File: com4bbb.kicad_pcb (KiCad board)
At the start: 2 copper layers, 54.6 x 86.4 mm, 51 parts, among them J101 RS485, J102 PWR, P8 BeagleBone_Black_Header, P9 BeagleBone_Black_Header, SW101 Reset, SW102 PWR, U101 ESP32-WROOM-32U, U102 SP3485EN, U103 AT24C512C-SSHD-T, U104 WPMDH1100xx1S

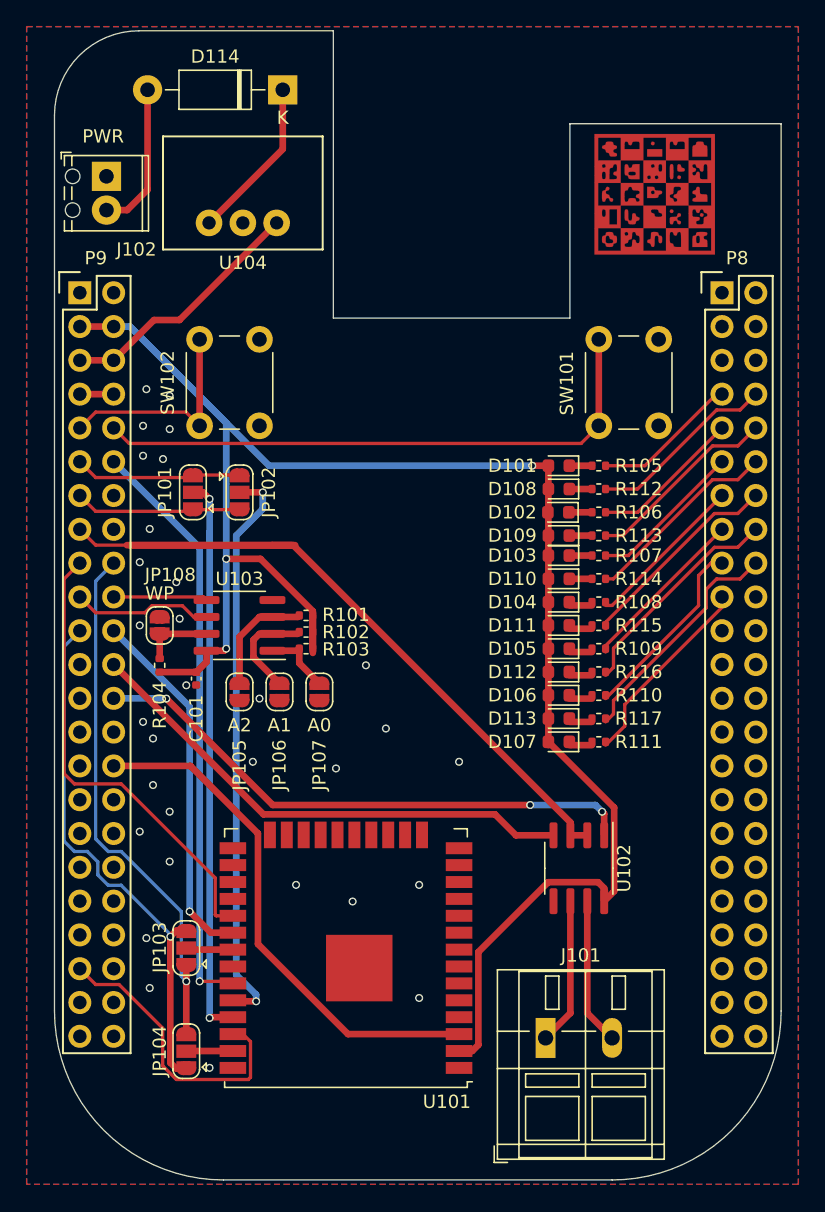
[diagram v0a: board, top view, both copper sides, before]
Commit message: Connect missing boot pin
The ESP32-wroom-32u module use IO0 to enter boot mode. In boot mode
the device can be flashed. Connect IO0 to the Beagle Bone to be able
to update firmware on demand.

Signed-off-by: Benedikt Spranger <b.spranger@linutronix.de>
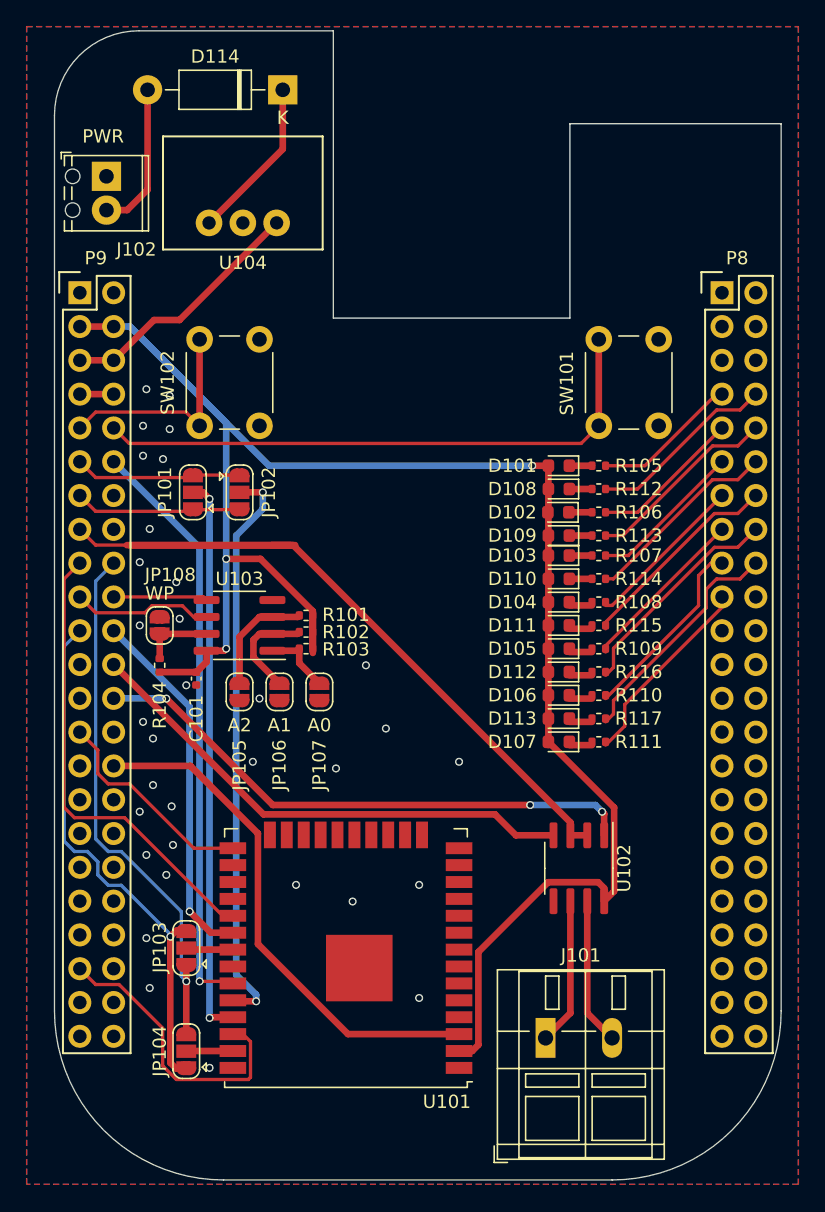
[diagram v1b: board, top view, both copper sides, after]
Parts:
- removed G***: LOGO, eurovibes:LOGO
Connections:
- net /GPIO_112 renamed /GPIO_122
- P9 pad 27: (no net) -> /GPIO_125
- U101 pad 25: (no net) -> /GPIO_125
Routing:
- net /GPIO_125: track 0.00 -> 16.1 mm
- net GNDD: vias 31 -> 33

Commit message: Update to KiCAD version 9
Signed-off-by: Benedikt Spranger <b.spranger@linutronix.de>
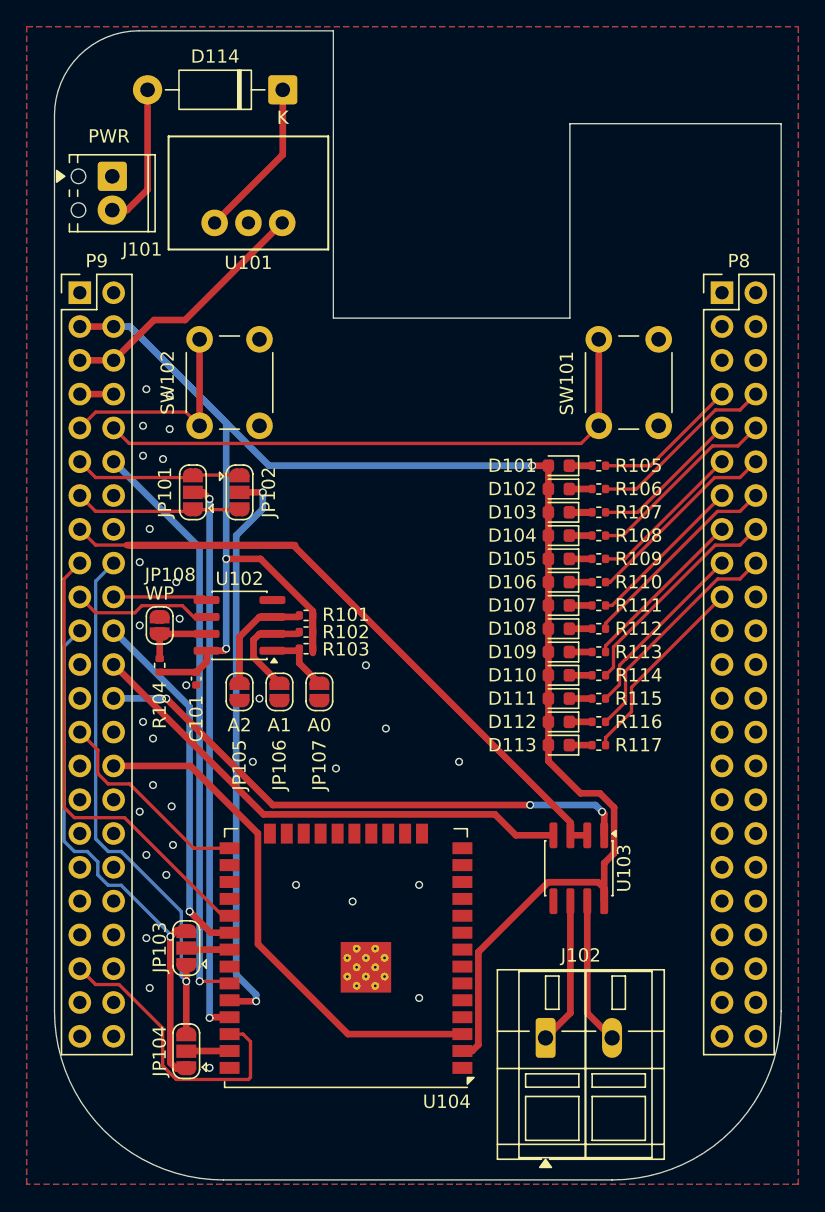
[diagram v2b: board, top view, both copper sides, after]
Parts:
- P8, P9: footprint Socket_BeagleBone_Black:Socket_BeagleBone_Black -> Connector_PinHeader_2.54mm:PinHeader_2x23_P2.54mm_Vertical
- moved D108 10.5 mm to (152.4, 87.6)
- moved R112 10.5 mm to (155.4, 87.6)
- moved D107 10.2 mm to (152.4, 85.9)
- moved R111 10.2 mm to (155.4, 85.9)
- moved D109 8.75 mm to (152.4, 89.4)
- moved R113 8.75 mm to (155.4, 89.4)
- moved D106 8.50 mm to (152.4, 84.1)
- moved R110 8.50 mm to (155.4, 84.1)
- moved D110 7.25 mm to (152.4, 91.1)
- moved R114 7.25 mm to (155.4, 91.1)
- moved D105 6.75 mm to (152.4, 82.4)
- moved R109 6.75 mm to (155.4, 82.4)
- moved D111 5.50 mm to (152.4, 92.9)
- moved R115 5.50 mm to (155.4, 92.9)
- moved D104 5.00 mm to (152.4, 80.6)
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- renumbered J102 to J101, J101 to J102, U104 to U101, U103 to U102, U102 to U103, U101 to U104
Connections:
- P8 pad 10: /LED8 -> /LED3
- P8 pad 11: /LED2 -> /LED4
- P8 pad 12: /LED9 -> /LED5
- P8 pad 13: /LED3 -> /LED6
- P8 pad 14: /LED10 -> /LED7
- P8 pad 15: /LED4 -> /LED8
- P8 pad 16: /LED11 -> /LED9
- P8 pad 17: /LED5 -> /LED10
- P8 pad 18: /LED12 -> /LED11
- P8 pad 19: /LED6 -> /LED12
- P8 pad 20: (no net) -> unconnected-(P8-Pin_20-Pad20)
- P8 pad 21: (no net) -> unconnected-(P8-Pin_21-Pad21)
- P8 pad 22: (no net) -> unconnected-(P8-Pin_22-Pad22)
- P8 pad 23: (no net) -> unconnected-(P8-Pin_23-Pad23)
- P8 pad 24: (no net) -> unconnected-(P8-Pin_24-Pad24)
- P8 pad 25: (no net) -> unconnected-(P8-Pin_25-Pad25)
- P8 pad 26: (no net) -> unconnected-(P8-Pin_26-Pad26)
- P8 pad 27: (no net) -> unconnected-(P8-Pin_27-Pad27)
- P8 pad 28: (no net) -> unconnected-(P8-Pin_28-Pad28)
- P8 pad 29: (no net) -> unconnected-(P8-Pin_29-Pad29)
- P8 pad 3: (no net) -> unconnected-(P8-Pin_3-Pad3)
- P8 pad 30: (no net) -> unconnected-(P8-Pin_30-Pad30)
- P8 pad 31: (no net) -> unconnected-(P8-Pin_31-Pad31)
- P8 pad 32: (no net) -> unconnected-(P8-Pin_32-Pad32)
- P8 pad 33: (no net) -> unconnected-(P8-Pin_33-Pad33)
- P8 pad 34: (no net) -> unconnected-(P8-Pin_34-Pad34)
- P8 pad 35: (no net) -> unconnected-(P8-Pin_35-Pad35)
- P8 pad 36: (no net) -> unconnected-(P8-Pin_36-Pad36)
- P8 pad 37: (no net) -> unconnected-(P8-Pin_37-Pad37)
- P8 pad 38: (no net) -> unconnected-(P8-Pin_38-Pad38)
- P8 pad 39: (no net) -> unconnected-(P8-Pin_39-Pad39)
- P8 pad 4: (no net) -> unconnected-(P8-Pin_4-Pad4)
- P8 pad 40: (no net) -> unconnected-(P8-Pin_40-Pad40)
- P8 pad 41: (no net) -> unconnected-(P8-Pin_41-Pad41)
- P8 pad 42: (no net) -> unconnected-(P8-Pin_42-Pad42)
- P8 pad 43: (no net) -> unconnected-(P8-Pin_43-Pad43)
- P8 pad 44: (no net) -> unconnected-(P8-Pin_44-Pad44)
- P8 pad 45: (no net) -> unconnected-(P8-Pin_45-Pad45)
- P8 pad 46: (no net) -> unconnected-(P8-Pin_46-Pad46)
- P8 pad 5: (no net) -> unconnected-(P8-Pin_5-Pad5)
- P8 pad 6: (no net) -> unconnected-(P8-Pin_6-Pad6)
- P8 pad 8: /LED7 -> /LED1
- P8 pad 9: /LED1 -> /LED2
- P9 pad 14: (no net) -> unconnected-(P9-Pin_14-Pad14)
- P9 pad 16: (no net) -> unconnected-(P9-Pin_16-Pad16)
- P9 pad 23: (no net) -> unconnected-(P9-Pin_23-Pad23)
- P9 pad 25: (no net) -> unconnected-(P9-Pin_25-Pad25)
- P9 pad 28: (no net) -> unconnected-(P9-Pin_28-Pad28)
- P9 pad 29: (no net) -> unconnected-(P9-Pin_29-Pad29)
- P9 pad 31: (no net) -> unconnected-(P9-Pin_31-Pad31)
- P9 pad 32: (no net) -> VDD_ADC
- P9 pad 33: (no net) -> unconnected-(P9-Pin_33-Pad33)
- P9 pad 34: (no net) -> GNDA_ADC
- P9 pad 35: (no net) -> unconnected-(P9-Pin_35-Pad35)
- P9 pad 36: (no net) -> unconnected-(P9-Pin_36-Pad36)
- P9 pad 37: (no net) -> unconnected-(P9-Pin_37-Pad37)
- P9 pad 38: (no net) -> unconnected-(P9-Pin_38-Pad38)
- P9 pad 39: (no net) -> unconnected-(P9-Pin_39-Pad39)
- P9 pad 40: (no net) -> unconnected-(P9-Pin_40-Pad40)
- P9 pad 42: (no net) -> unconnected-(P9-Pin_42-Pad42)
- U104 pad 10: (no net) -> unconnected-(U104-IO25-Pad10)
- U104 pad 11: (no net) -> unconnected-(U104-IO26-Pad11)
- U104 pad 12: (no net) -> unconnected-(U104-IO27-Pad12)
- U104 pad 13: (no net) -> unconnected-(U104-IO14-Pad13)
- U104 pad 14: (no net) -> unconnected-(U104-IO12-Pad14)
- U104 pad 16: (no net) -> unconnected-(U104-IO13-Pad16)
- U104 pad 17: (no net) -> unconnected-(U104-SHD/SD2-Pad17)
- U104 pad 18: (no net) -> unconnected-(U104-SWP/SD3-Pad18)
- U104 pad 19: (no net) -> unconnected-(U104-SCS/CMD-Pad19)
- U104 pad 20: (no net) -> unconnected-(U104-SCK/CLK-Pad20)
- U104 pad 21: (no net) -> unconnected-(U104-SDO/SD0-Pad21)
- U104 pad 22: (no net) -> unconnected-(U104-SDI/SD1-Pad22)
- U104 pad 23: (no net) -> unconnected-(U104-IO15-Pad23)
- U104 pad 24: (no net) -> unconnected-(U104-IO2-Pad24)
- U104 pad 26: (no net) -> unconnected-(U104-IO4-Pad26)
- U104 pad 27: (no net) -> unconnected-(U104-IO16-Pad27)
- U104 pad 28: (no net) -> unconnected-(U104-IO17-Pad28)
- U104 pad 32: (no net) -> unconnected-(U104-NC-Pad32)
- U104 pad 4: (no net) -> unconnected-(U104-SENSOR_VP-Pad4)
- U104 pad 5: (no net) -> unconnected-(U104-SENSOR_VN-Pad5)
- U104 pad 6: (no net) -> unconnected-(U104-IO34-Pad6)
- U104 pad 7: (no net) -> unconnected-(U104-IO35-Pad7)
- U104 pad 8: (no net) -> unconnected-(U104-IO32-Pad8)
- U104 pad 9: (no net) -> unconnected-(U104-IO33-Pad9)
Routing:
- net /LED12: track 17.6 -> 14.8 mm
- net /LED1: track 11.4 -> 14.2 mm
- net /LED6: track 14.8 -> 12.2 mm
- net /LED3: track 12.2 -> 14.6 mm
- net /LED10: track 15.7 -> 13.8 mm
- net /LED8: track 14.6 -> 12.8 mm
- net /LED9: track 14.9 -> 16.7 mm
- net Net-(D103-K): track 1.70 -> 3.44 mm
- net /GPIO_48: track 62.3 -> 60.9 mm
- net /LED7: track 14.2 -> 15.7 mm
- net /LED4: track 12.8 -> 11.8 mm
- net /LED11: track 16.7 -> 17.6 mm
- net /SPI0_CS0: track 34.9 -> 34.1 mm
- net Net-(J102-Pin_2): track 11.8 -> 11.0 mm
- net Net-(JP101-C): track 43.0 -> 42.2 mm
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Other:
- outline, holes or cut-outs redrawn
- net class Default removed

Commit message: Update to ESP32-S3-WROOM-1U
Signed-off-by: Benedikt Spranger <bene@eurovibes.org>
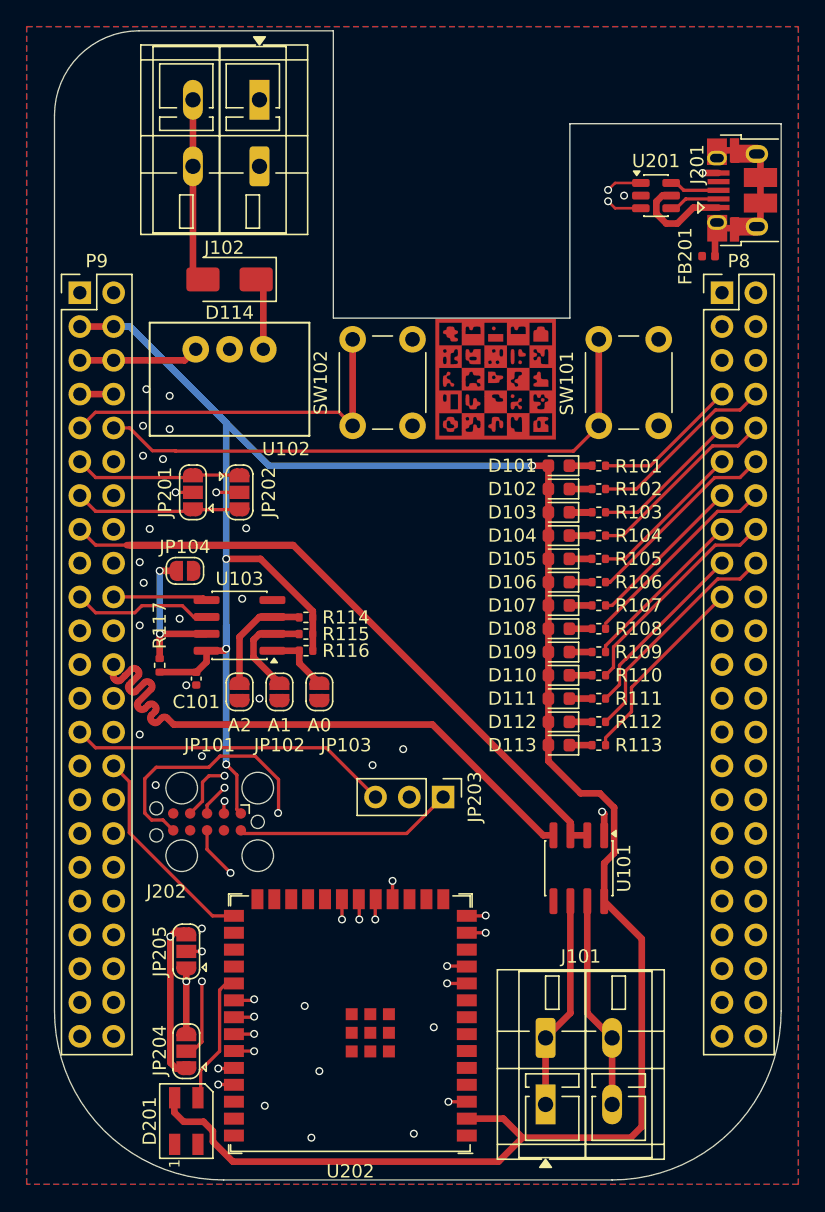
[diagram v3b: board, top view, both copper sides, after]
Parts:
- removed JP108: WP, Jumper:SolderJumper-2_P1.3mm_Open_RoundedPad1.0x1.5mm
- removed U104: ESP32-WROOM-32U, RF_Module:ESP32-WROOM-32U
- added D201: SK6812MINI, LED_SMD:LED_SK6812MINI_PLCC4_3.5x3.5mm_P1.75mm, F.Cu at (124.4, 124.6)
- added FB201: FerriteBead_Small, Inductor_SMD:L_0402_1005Metric, F.Cu at (163.6, 59.6)
- added G***: LOGO, eurovibes:LOGO, F.Cu at (147.6, 68.9)
- added J201: USB_B_Micro, Connector_USB:USB_Micro-B_Amphenol_10103594-0001LF_Horizontal, F.Cu at (166.1, 54.7)
- added J202: JTAG, Connector:Tag-Connect_TC2050-IDC-FP_2x05_P1.27mm_Vertical, F.Cu at (125.9, 102.1)
- added JP104: WP, Jumper:SolderJumper-2_P1.3mm_Open_RoundedPad1.0x1.5mm, F.Cu at (124.3, 83.3)
- added JP203: JTAG, Connector_PinHeader_2.54mm:PinHeader_1x03_P2.54mm_Vertical, F.Cu at (143.7, 100.3)
- added U201: USBLC6-2SC6, Package_TO_SOT_SMD:SOT-23-6, F.Cu at (159.7, 55.1)
- added U202: ESP32-S3-WROOM-1, PCM_Espressif:ESP32-S3-WROOM-1U, F.Cu at (136.7, 117.5)
- D114: value 1N4004 -> MRA4004T3G; footprint Diode_THT:D_DO-41_SOD81_P10.16mm_Horizontal -> Diode_SMD:D_SMA
- J101: renamed from J102; footprint TerminalBlock_WAGO:TerminalBlock_WAGO_236-102_1x02_P5.00mm_45Degree -> TerminalBlock_WAGO:TerminalBlock_WAGO_236-402_1x02_P5.00mm_45Degree
- J102: renamed from J101; footprint TerminalBlock_Phoenix:TerminalBlock_Phoenix_MPT-0,5-2-2.54_1x02_P2.54mm_Horizontal -> TerminalBlock_WAGO:TerminalBlock_WAGO_236-402_1x02_P5.00mm_45Degree
- moved R104 34.4 mm to (155.4, 80.6), turned to 0 degrees
- moved R117 33.5 mm to (122.4, 90.4), turned to 90 degrees
- moved R101 24.7 mm to (155.4, 75.4), turned to 0 degrees
- moved R102 24.5 mm to (155.4, 77.1), turned to 0 degrees
- moved R103 24.3 mm to (155.4, 78.9), turned to 0 degrees
- moved R116 22.6 mm to (133.4, 89.3), turned to 180 degrees
- moved R115 22.5 mm to (133.4, 88.0), turned to 180 degrees
- moved R114 22.4 mm to (133.4, 86.8), turned to 180 degrees
- moved D114 14.8 mm to (127.6, 61.4)
- moved SW102 11.5 mm to (136.9, 72.4)
- moved J102 11.1 mm to (129.9, 52.9), turned to 180 degrees
- moved U102 9.61 mm to (127.6, 66.6), turned to 180 degrees
- moved JP204 7.75 mm to (124.4, 119.4)
- moved JP205 7.50 mm to (124.4, 111.9)
- moved R105 7.00 mm to (155.4, 82.4)
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- renumbered JP105 to JP101, JP106 to JP102, JP107 to JP103, JP101 to JP201, JP102 to JP202, JP103 to JP204, JP104 to JP205, U103 to U101, U101 to U102, U102 to U103
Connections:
- JP101 pad 1: Net-(JP105-A) -> Net-(JP101-A)
- JP102 pad 1: Net-(JP106-A) -> Net-(JP102-A)
- JP103 pad 1: Net-(JP107-A) -> Net-(JP103-A)
- JP204 pad 1: /SPI0_D1 -> /SPI0_D0
- JP204 pad 3: /SPI0_D0 -> /SPI0_D1
- JP205 pad 1: /SPI0_D0 -> /SPI0_D1
- JP205 pad 3: /SPI0_D1 -> /SPI0_D0
- R101 pad 1: +3V3 -> Net-(D101-K)
- R101 pad 2: Net-(JP105-A) -> /LED0
- R102 pad 1: +3V3 -> Net-(D102-K)
- R102 pad 2: Net-(JP106-A) -> /LED1
- R103 pad 1: +3V3 -> Net-(D103-K)
- R103 pad 2: Net-(JP107-A) -> /LED2
- R104 pad 1: +3V3 -> Net-(D104-K)
- R104 pad 2: Net-(JP108-A) -> /LED3
- R105 pad 1: Net-(D101-K) -> Net-(D105-K)
- R105 pad 2: /LED0 -> /LED4
- R106 pad 1: Net-(D102-K) -> Net-(D106-K)
- R106 pad 2: /LED1 -> /LED5
- R107 pad 1: Net-(D103-K) -> Net-(D107-K)
- R107 pad 2: /LED2 -> /LED6
- R108 pad 1: Net-(D104-K) -> Net-(D108-K)
- R108 pad 2: /LED3 -> /LED7
- R109 pad 1: Net-(D105-K) -> Net-(D109-K)
- R109 pad 2: /LED4 -> /LED8
- R110 pad 1: Net-(D106-K) -> Net-(D110-K)
- R110 pad 2: /LED5 -> /LED9
- R111 pad 1: Net-(D107-K) -> Net-(D111-K)
- R111 pad 2: /LED6 -> /LED10
- R112 pad 1: Net-(D108-K) -> Net-(D112-K)
- R112 pad 2: /LED7 -> /LED11
- R113 pad 1: Net-(D109-K) -> Net-(D113-K)
- R113 pad 2: /LED8 -> /LED12
- R114 pad 1: Net-(D110-K) -> +3V3
- R114 pad 2: /LED9 -> Net-(JP101-A)
- R115 pad 1: Net-(D111-K) -> +3V3
- R115 pad 2: /LED10 -> Net-(JP102-A)
- R116 pad 1: Net-(D112-K) -> +3V3
- R116 pad 2: /LED11 -> Net-(JP103-A)
- R117 pad 1: Net-(D113-K) -> +3V3
- R117 pad 2: /LED12 -> Net-(JP104-A)
- U103 pad 1: Net-(JP107-A) -> Net-(JP103-A)
- U103 pad 2: Net-(JP106-A) -> Net-(JP102-A)
- U103 pad 3: Net-(JP105-A) -> Net-(JP101-A)
- U103 pad 7: Net-(JP108-A) -> Net-(JP104-A)
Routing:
- net /ESP32/D-: track 0.00 -> 64.1 mm, vias 0 -> 2
- net /ESP32/D+: track 0.00 -> 64.1 mm, vias 0 -> 2
- net +3V3: track 144.1 -> 205.6 mm, vias 3 -> 4
- net /ESP32/TDO: track 0.00 -> 36.9 mm, vias 0 -> 2
- net Net-(JP203-C): track 0.00 -> 25.6 mm, vias 0 -> 1
- net /ESP32/TCK: track 0.00 -> 23.9 mm, vias 0 -> 2
- net /ESP32/TMS: track 0.00 -> 23.5 mm, vias 0 -> 2
- net /GPIO_122: track 39.2 -> 16.0 mm
- net Net-(JP204-C): track 3.38 -> 22.5 mm, vias 0 -> 2
- net /ESP32/TDI: track 0.00 -> 18.3 mm, vias 0 -> 2
- net /ESP32/~{RST}: track 0.00 -> 16.4 mm
- net /SPI0_SCLK: track 27.4 -> 39.3 mm, vias 1 -> 2
- net PWR_BUT: track 16.4 -> 27.9 mm
- net Net-(JP104-A): track 0.00 -> 11.3 mm, vias 0 -> 2
- net Net-(JP205-C): track 3.48 -> 14.2 mm, vias 0 -> 2
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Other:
- copper layers 2 -> 4
